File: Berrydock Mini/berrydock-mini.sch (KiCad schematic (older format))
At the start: 90 parts, among them J1 RJ45, P1 CONN_01X18, P2 CONN_01X18, P3 CONN_01X04, P4 CONN_01X02, P5 USB_OTG, P6 USB_A, SW1 SWITCH_INV, SW2 BUTTON, U1 USBLC6-2, U10 MCP73831, U11 FS8205A, U12 DW01-P, U13 USBLC6-2, U14 ADS1015, U15 USBLC6-2, U16 CP2102, U2 USBLC6-2, U3 AMS1117, U4 H1260NL, U5 Omega2, U6 SMP75, U7 SMP75, U8 ACT4088, U9 L6920DC

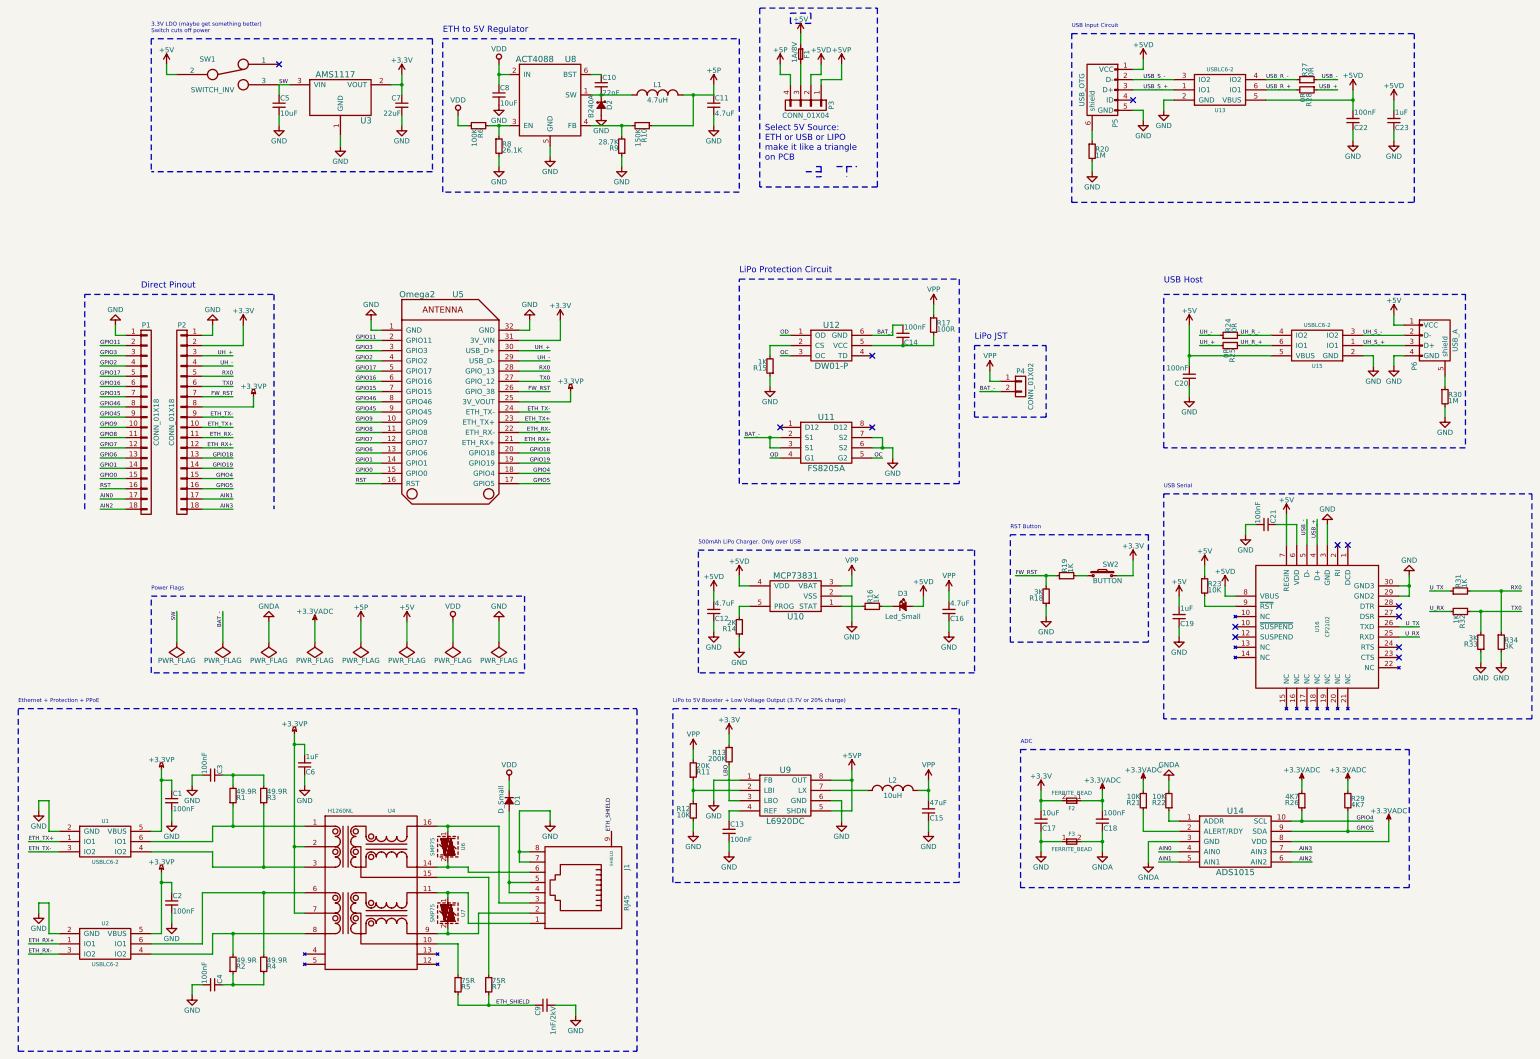
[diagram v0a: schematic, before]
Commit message: Connected Power Pins to GPIO for charge/low voltage on LiPo
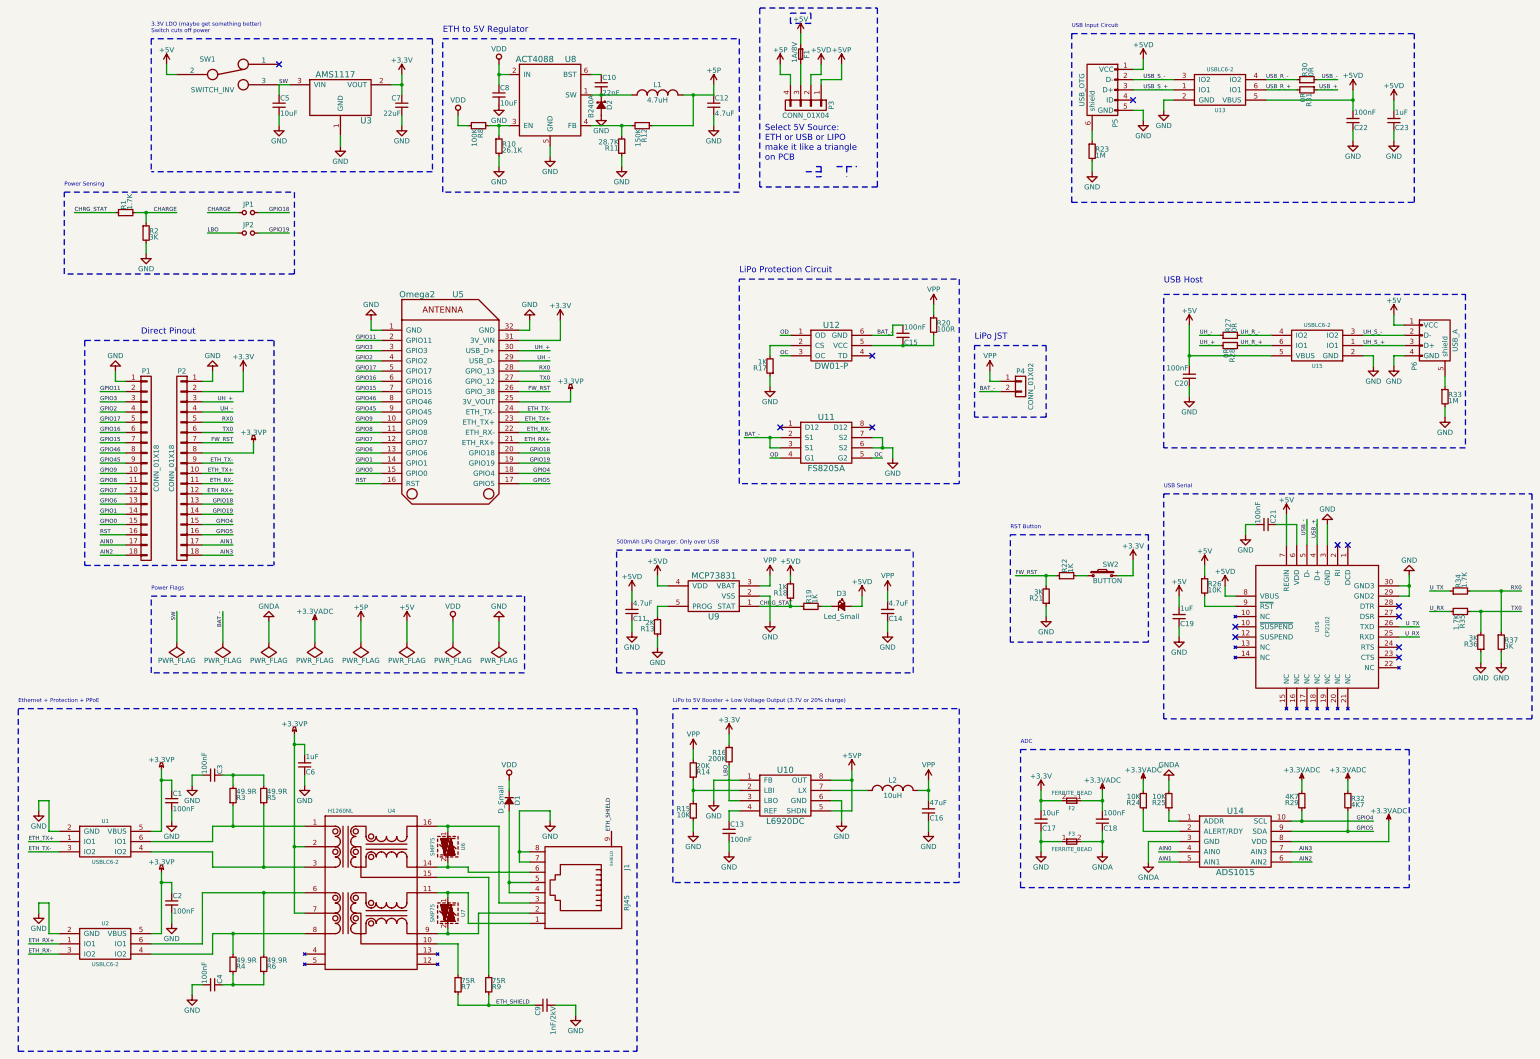
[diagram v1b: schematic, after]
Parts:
- added JP1, JP2: Jumper_NO_Small, symbol Jumper_NO_Small
- added R1: 1.7K, symbol R_Small
- added R18: 1K, symbol R_Small
- added R2: 3K, symbol R_Small
- R34: renamed from R31; value 1K -> 1.7K
- R35: renamed from R32; value 1K -> 1.7K
- renumbered C12 to C11, C11 to C12, C16 to C14, C14 to C15, C15 to C16, R8 to R10, R9 to R11, R10 to R12, R14 to R13, R11 to R14, R12 to R15, R13 to R16, R15 to R17, R16 to R19, R17 to R20, R18 to R21, R19 to R22, R20 to R23, R21 to R24, R22 to R25, R23 to R26, R24 to R27, R25 to R28, R26 to R29, R1 to R3, R27 to R30, R28 to R31, R29 to R32, R30 to R33, R33 to R36, R34 to R37, R2 to R4, R3 to R5, R4 to R6, R5 to R7, R6 to R8, R7 to R9, U9 to U10, U10 to U9
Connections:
- net +5VD: now also R18.2
- net GND: now also R2.2
- net GPIO18: now also JP1.2
- net GPIO19: now also JP2.2
- net LBO: now also JP2.1
- net CHRG_STAT: now reaches R19.1, U9.1 (STAT)
- net CHRG_STAT: now also R1.1, R18.1
- new net CHARGE: JP1.1, R1.2, R2.1
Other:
- note added: "Power Sensing"
- moved on the sheet: C11, C14, D3, P1, P2, R13, R19, U9

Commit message: changed some resistor values
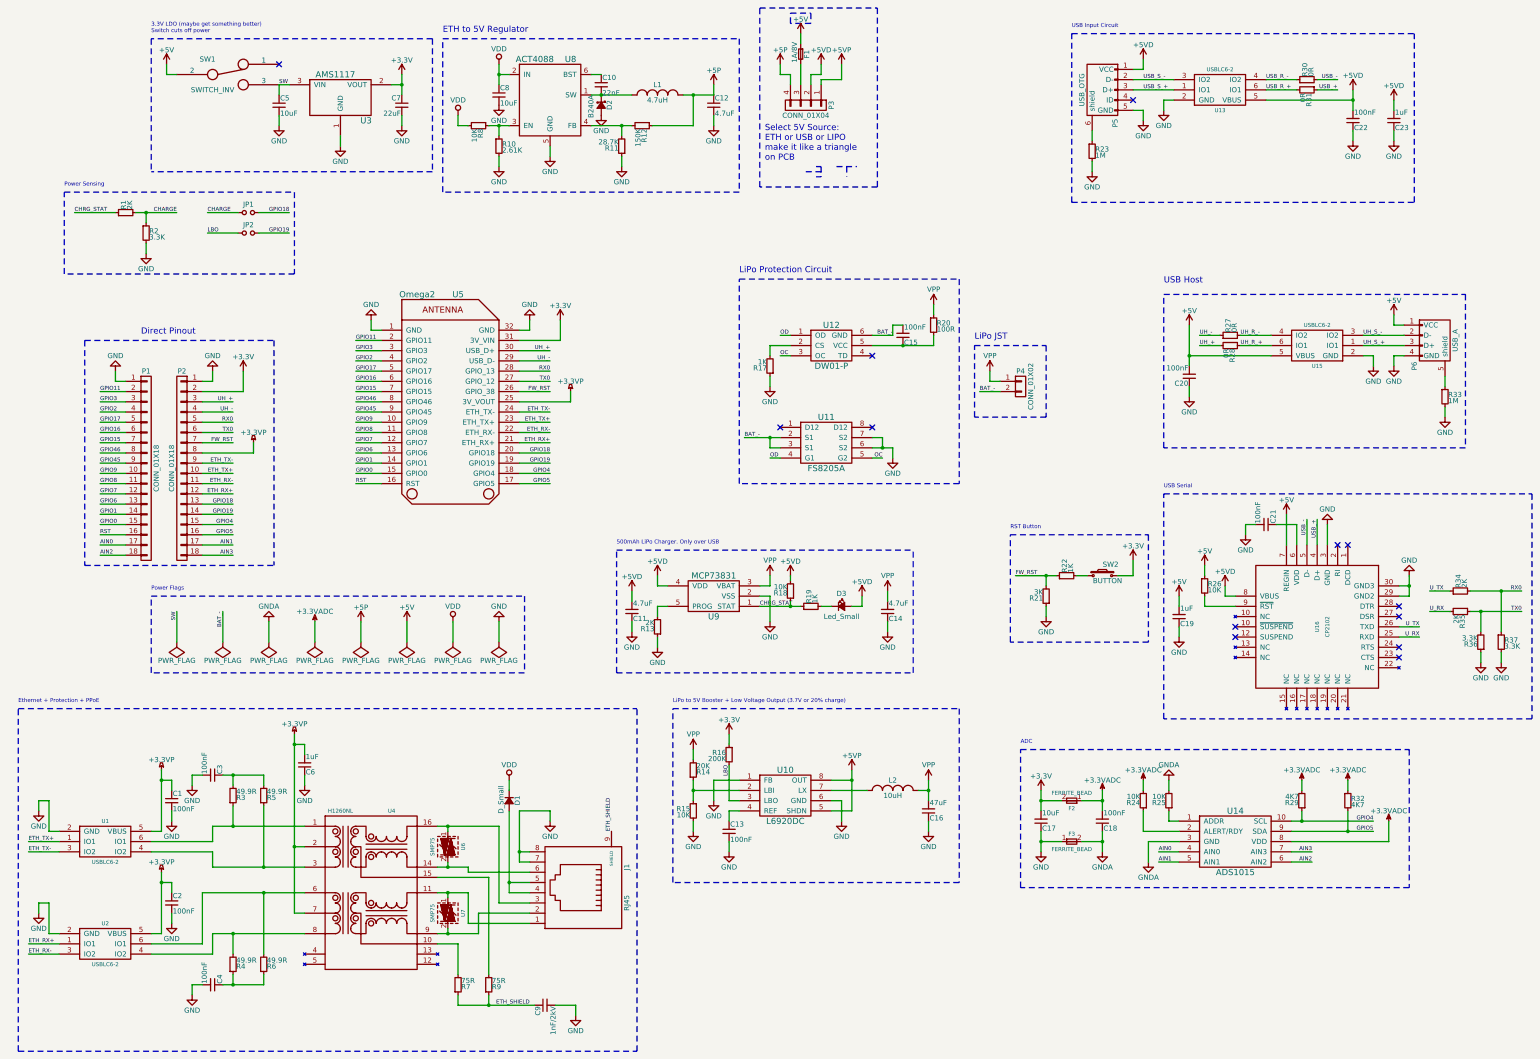
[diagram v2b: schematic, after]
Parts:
- R1, R34, R35: value 1.7K -> 2K
- R10: value 26.1K -> 2.61K
- R18: value 1K -> 10K
- R2, R36, R37: value 3K -> 3.3K
- R8: value 100K -> 10K
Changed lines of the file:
@@
 P 5350 1900
 F 0 "R8" H 5380 1920 50  0000 L CNN
-F 1 "100K" H 5380 1860 50  0000 L CNN
+F 1 "10K" H 5380 1860 50  0000 L CNN
 F 2 "" H 5350 1900 50  0000 C CNN
 F 3 "" H 5350 1900 50  0000 C CNN
@@
 P 5550 2100
 F 0 "R10" H 5580 2120 50  0000 L CNN
-F 1 "26.1K" H 5580 2060 50  0000 L CNN
+F 1 "2.61K" H 5580 2060 50  0000 L CNN
 F 2 "" H 5550 2100 50  0000 C CNN
 F 3 "" H 5550 2100 50  0000 C CNN
@@
 P 15150 6950
 F 0 "R36" H 15180 6970 50  0000 L CNN
-F 1 "3K" H 15180 6910 50  0000 L CNN
+F 1 "3.3K" H 15180 6910 50  0000 L CNN
 F 2 "" H 15150 6950 50  0000 C CNN
 F 3 "" H 15150 6950 50  0000 C CNN
@@
 P 15350 6950
 F 0 "R37" H 15380 6970 50  0000 L CNN
-F 1 "3K" H 15380 6910 50  0000 L CNN
+F 1 "3.3K" H 15380 6910 50  0000 L CNN
 F 2 "" H 15350 6950 50  0000 C CNN
 F 3 "" H 15350 6950 50  0000 C CNN
@@
 P 14950 6650
 F 0 "R35" H 14980 6670 50  0000 L CNN
-F 1 "1.7K" H 14980 6610 50  0000 L CNN
+F 1 "2K" H 14980 6610 50  0000 L CNN
 F 2 "" H 14950 6650 50  0000 C CNN
 F 3 "" H 14950 6650 50  0000 C CNN
@@
 P 14950 6450
 F 0 "R34" H 14980 6470 50  0000 L CNN
-F 1 "1.7K" H 14980 6410 50  0000 L CNN
+F 1 "2K" H 14980 6410 50  0000 L CNN
 F 2 "" H 14950 6450 50  0000 C CNN
 F 3 "" H 14950 6450 50  0000 C CNN
@@
 P 8400 6450
 F 0 "R18" H 8430 6470 50  0000 L CNN
-F 1 "1K" H 8430 6410 50  0000 L CNN
+F 1 "10K" H 8430 6410 50  0000 L CNN
 F 2 "" H 8400 6450 50  0000 C CNN
 F 3 "" H 8400 6450 50  0000 C CNN
@@
 P 1900 2750
 F 0 "R1" H 1930 2770 50  0000 L CNN
-F 1 "1.7K" H 1930 2710 50  0000 L CNN
+F 1 "2K" H 1930 2710 50  0000 L CNN
 F 2 "" H 1900 2750 50  0000 C CNN
 F 3 "" H 1900 2750 50  0000 C CNN
@@
 P 2100 2950
 F 0 "R2" H 2130 2970 50  0000 L CNN
-F 1 "3K" H 2130 2910 50  0000 L CNN
+F 1 "3.3K" H 2130 2910 50  0000 L CNN
 F 2 "" H 2100 2950 50  0000 C CNN
 F 3 "" H 2100 2950 50  0000 C CNN

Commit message: added some footprints
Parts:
- added C?: 4.7uF, Capacitors_SMD:C_0603, symbol C_Small
- C10, C12, C13, C14, C17, C18, C19, C2, C21, C22, C3, C4, C5, C7: footprint (none) -> Capacitors_SMD:C_0603
- C15: value 100nF -> Capacitors_SMD:C_0603
- C16: footprint (none) -> Capacitors_SMD:C_0805
- C23: value 1uF -> 4.7uF; footprint (none) -> Capacitors_SMD:C_0603
- C8, C9: footprint (none) -> Capacitors_SMD:C_1206
- P1, P2: footprint (none) -> Pin_Headers:Pin_Header_Straight_1x18
- R1, R10, R11, R12, R13, R14, R15, R16, R17, R18, R19, R2, R20, R21, R22, R23, R24, R25, R26, R27, R28, R29, R3, R30, R31, R32, R33, R34, R35, R36, R37, R4, R5, R6, R7, R8, R9: footprint (none) -> Resistors_SMD:R_0603_HandSoldering
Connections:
- net +5VD: now also C?.2
- net GND: now also C?.1

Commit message: changed annontation
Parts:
- gave numbers to parts that had none: 1
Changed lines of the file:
@@
 Power Sensing
 $Comp
-L C_Small C?
+L C_Small C24
 U 1 1 57EADFA6
 P 15200 4300
-F 0 "C?" H 15210 4370 50  0000 L CNN
+F 0 "C24" H 15210 4370 50  0000 L CNN
 F 1 "4.7uF" H 15210 4220 50  0000 L CNN
 F 2 "Capacitors_SMD:C_0603" H 15200 4300 50  0001 C CNN
@@
 $EndComp
 $Comp
-L +5VD #PWR?
+L +5VD #PWR0114
 U 1 1 57EADFAC
 P 15200 4100
-F 0 "#PWR?" H 15200 3950 50  0001 C CNN
+F 0 "#PWR0114" H 15200 3950 50  0001 C CNN
 F 1 "+5VD" H 15200 4240 50  0000 C CNN
 F 2 "" H 15200 4100 50  0000 C CNN
@@
 	15200 4100 15200 4200
 $Comp
-L GND #PWR?
+L GND #PWR0115
 U 1 1 57EADFB3
 P 15200 4500
-F 0 "#PWR?" H 15200 4250 50  0001 C CNN
+F 0 "#PWR0115" H 15200 4250 50  0001 C CNN
 F 1 "GND" H 15200 4350 50  0000 C CNN
 F 2 "" H 15200 4500 50  0000 C CNN
